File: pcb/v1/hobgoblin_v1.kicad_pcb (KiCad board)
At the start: 2 copper layers, 160 x 115 mm, 60 parts, among them J1 5V, J2 RC2014EXT1, J3 RC2014EXT2, J4 USB_B_Mini, J5 UART, SW1 RESET, SW2 ROMBNK, U1 74LS32, U10 FT232RL, U2 Z80CPU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

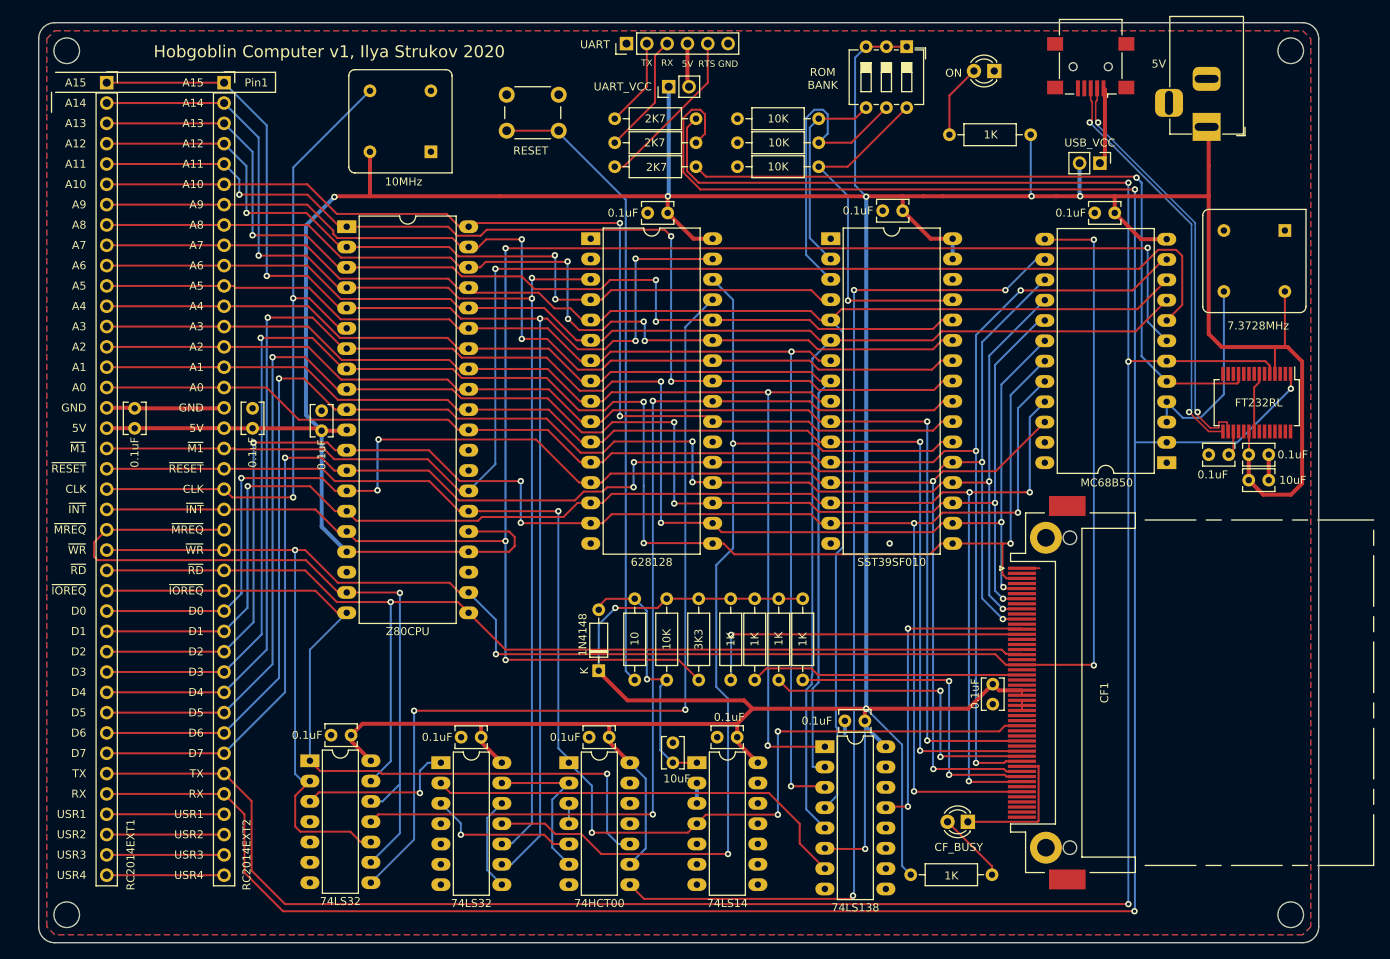
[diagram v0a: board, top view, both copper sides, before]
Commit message: Fix the CF card slot footprint (v1.1.)
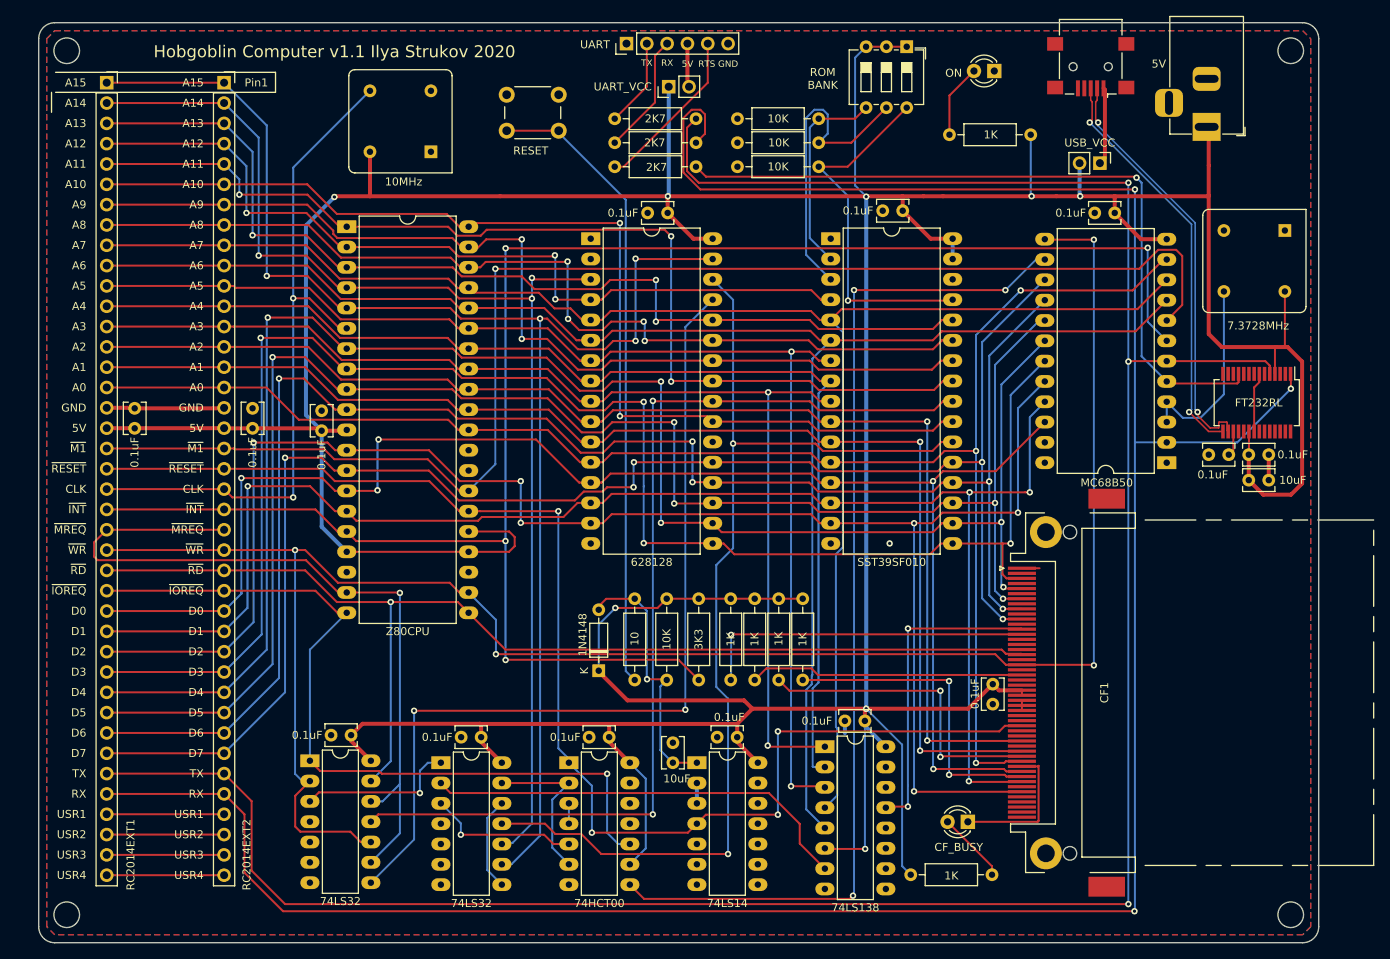
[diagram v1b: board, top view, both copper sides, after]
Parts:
- CF1: footprint Connector_Card:CF-Card_3M_N7E50-7516PK-20-WF -> hobgoblin:CF-Card_3M_N7E50-7516PK-20-WF
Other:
- rule pad_to_mask_clearance: 0.05 -> 0
- board text added: "Hobgoblin Computer v1.1 Ilya Strukov 2020"
- board text removed: "Hobgoblin Computer v1, Ilya Strukov 2020"

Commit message: Fix CF footprint pin numbering
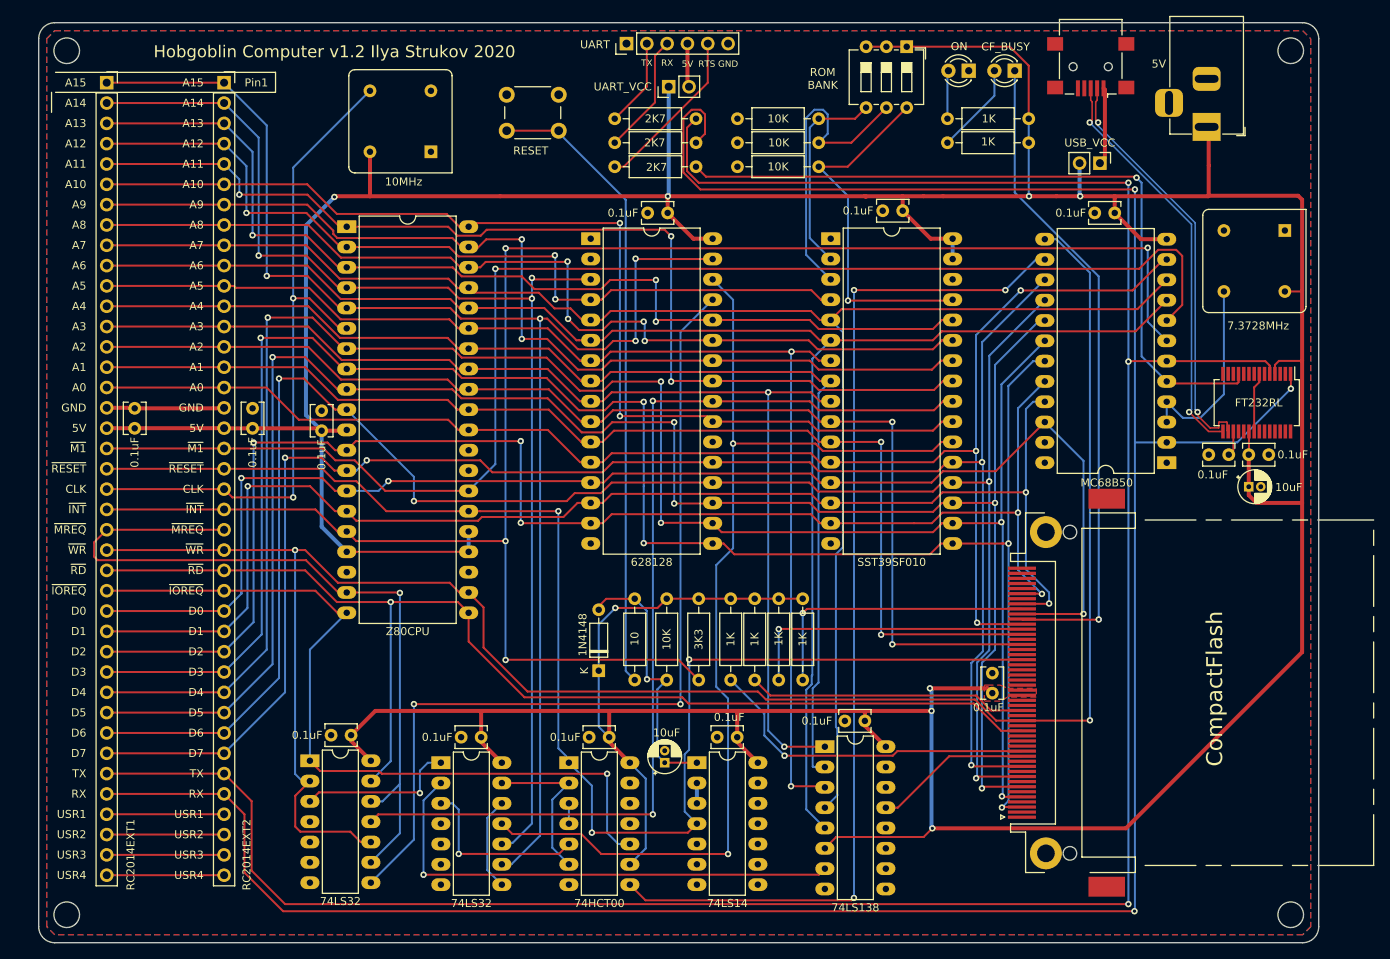
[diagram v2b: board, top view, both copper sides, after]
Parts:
- C1, C13: footprint Capacitor_THT:C_Disc_D3.8mm_W2.6mm_P2.50mm -> Capacitor_THT:CP_Radial_D4.0mm_P1.50mm
- moved D2 94.1 mm to (142.0, 26.0)
- moved R15 92.7 mm to (143.8, 35.0), turned to 180 degrees
- moved D5 3.20 mm to (136.2, 26.0)
- moved R11 2.02 mm to (143.8, 32.0)
- moved C16 1.12 mm to (139.2, 103.8), turned to 90 degrees
- moved C1 1.02 mm to (98.2, 112.5)
- moved C13 0.82 mm to (171.3, 78.0)
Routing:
- net Net-(CF1-Pad45): track 17.9 -> 82.6 mm, vias 0 -> 1
- net /D3: track 206.2 -> 236.3 mm, vias 4 -> 5
- net /D2: track 211.5 -> 182.3 mm, vias 6 -> 5
- net /D5: track 208.0 -> 234.7 mm
- net /D4: track 213.9 -> 240.2 mm
- net /D6: track 205.7 -> 229.8 mm, vias 5 -> 4
- net /D1: track 190.9 -> 167.2 mm, vias 4 -> 3
- net /D0: track 193.8 -> 172.3 mm, vias 5 -> 3
- net /~PORT10: track 39.4 -> 19.7 mm, vias 2 -> 0
- net VCC: track 674.4 -> 654.9 mm
- net /D7: track 198.0 -> 216.1 mm, vias 5 -> 4
- net /A0: track 201.1 -> 183.5 mm
- net /A1: track 158.1 -> 143.6 mm
- net /A2: track 159.4 -> 147.3 mm
- net /~RESET: track 166.0 -> 177.2 mm, vias 4 -> 3
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- added copper zone on F.Cu, net VCC
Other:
- board text added: "CompactFlash"
- board text added: "Hobgoblin Computer v1.2 Ilya Strukov 2020"
- board text removed: "Hobgoblin Computer v1.1 Ilya Strukov 2020"

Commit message: Reroute USB diff pair
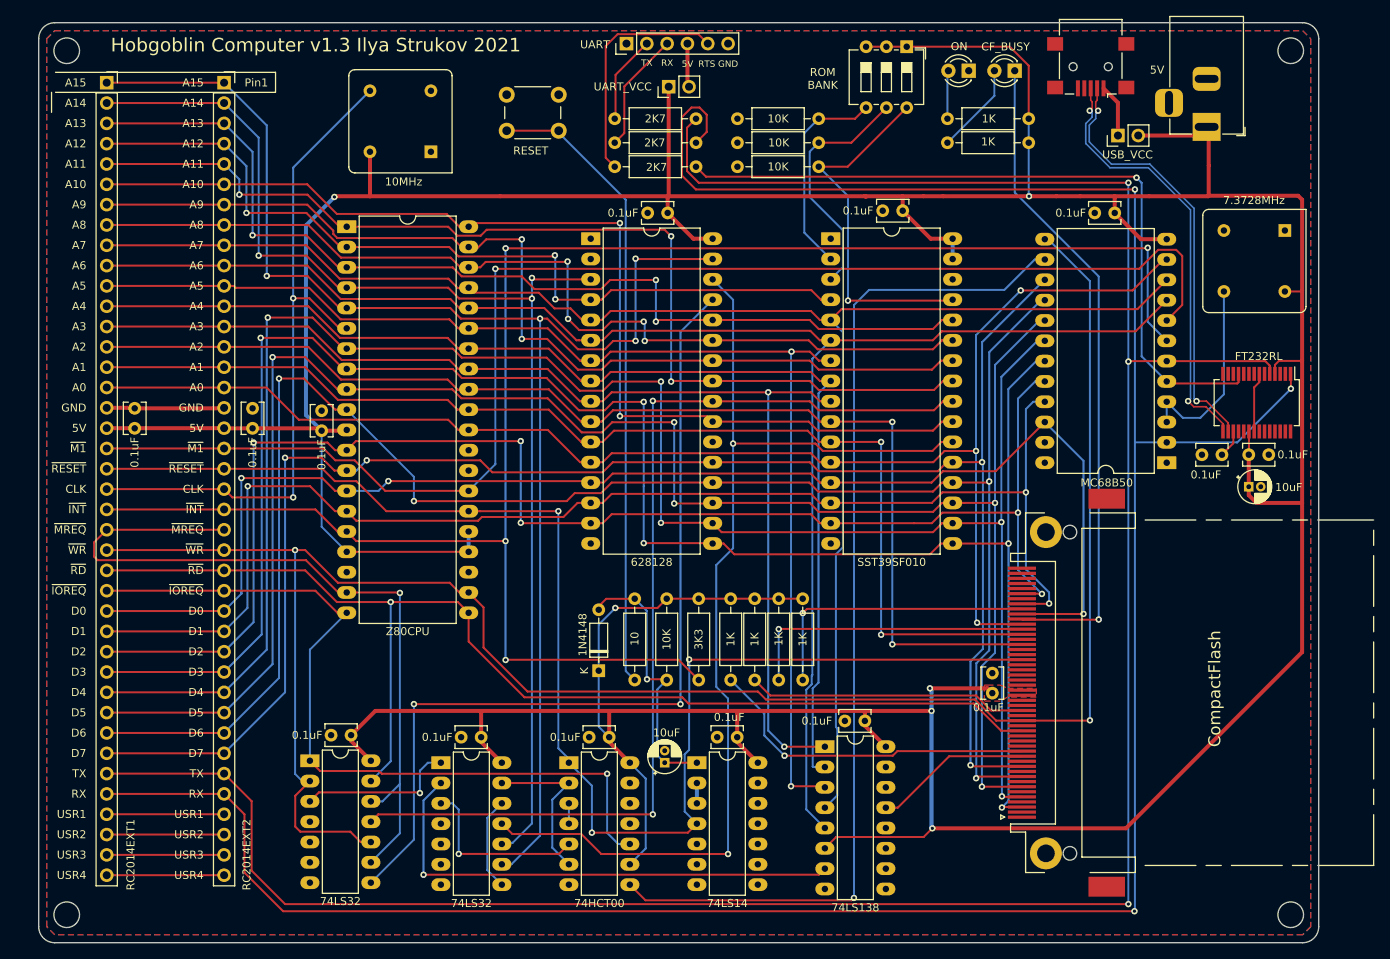
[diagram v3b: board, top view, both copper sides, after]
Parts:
- moved JP1 4.12 mm to (154.9, 34.1), turned to 90 degrees
- moved C15 0.85 mm to (165.4, 74.0)
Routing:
- net /ROMBNK1: track 39.1 -> 30.2 mm
- net Net-(J5-Pad5): track 20.9 -> 29.4 mm
- net VCC: track 654.9 -> 659.8 mm, vias 8 -> 6
- net /USB_UART/USBD+: track 51.3 -> 54.6 mm
- net Net-(J4-Pad1): track 9.69 -> 6.65 mm
- net /USB_UART/USBD-: track 52.5 -> 54.3 mm
- net /RXD: track 324.7 -> 325.9 mm
- net /IORQ: track 130.4 -> 129.3 mm, vias 3 -> 1
- net /D2: track 182.3 -> 183.0 mm
- net /~WR: track 244.9 -> 244.3 mm
- net /ROMBNK2: track 25.6 -> 26.1 mm
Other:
- board text added: "Hobgoblin Computer v1.3 Ilya Strukov 2021"
- board text removed: "Hobgoblin Computer v1.2 Ilya Strukov 2020"

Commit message: Fix IOWR/IORD pins on CF socket
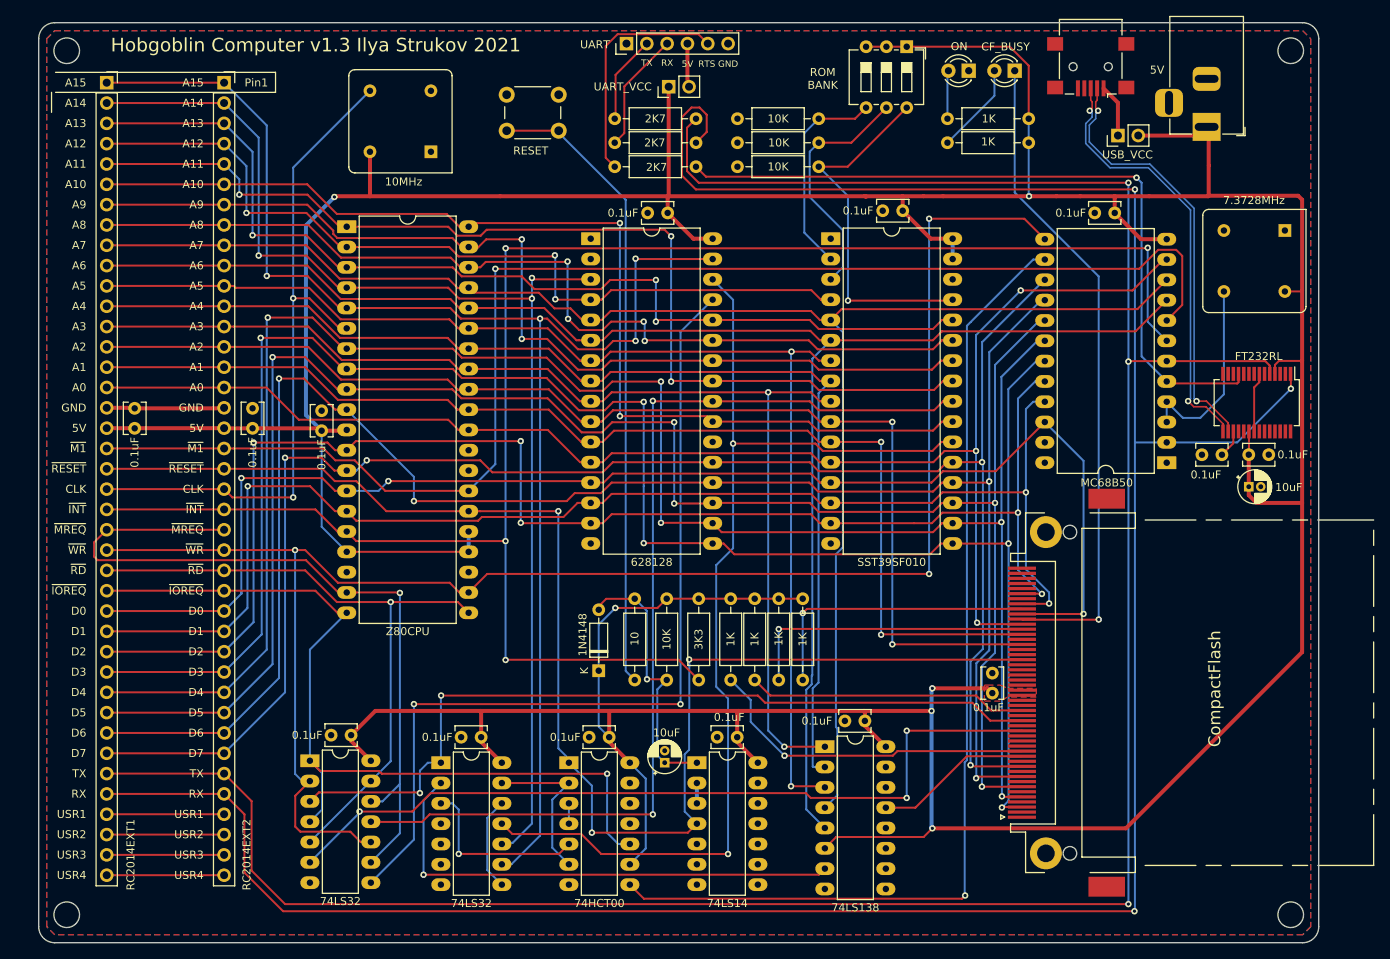
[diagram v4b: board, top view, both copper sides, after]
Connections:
- CF1 pad 34: /~RD -> /~IORD
- CF1 pad 35: /~WR -> /~IOWR
- U1 pad 4: (no net) -> /~IORQ
- U1 pad 5: (no net) -> /~RD
- U1 pad 6: (no net) -> /~IORD
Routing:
- net /~IORD: track 0.00 -> 101.3 mm, vias 0 -> 3
- net /~IOWR: track 20.1 -> 102.4 mm, vias 1 -> 2
- net /~RD: track 148.2 -> 81.6 mm
- net /~WR: track 244.3 -> 212.8 mm, vias 2 -> 3
- net /~IORQ: track 100.6 -> 109.5 mm
- net /IORQ: track 129.3 -> 127.3 mm

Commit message: Clean up routing
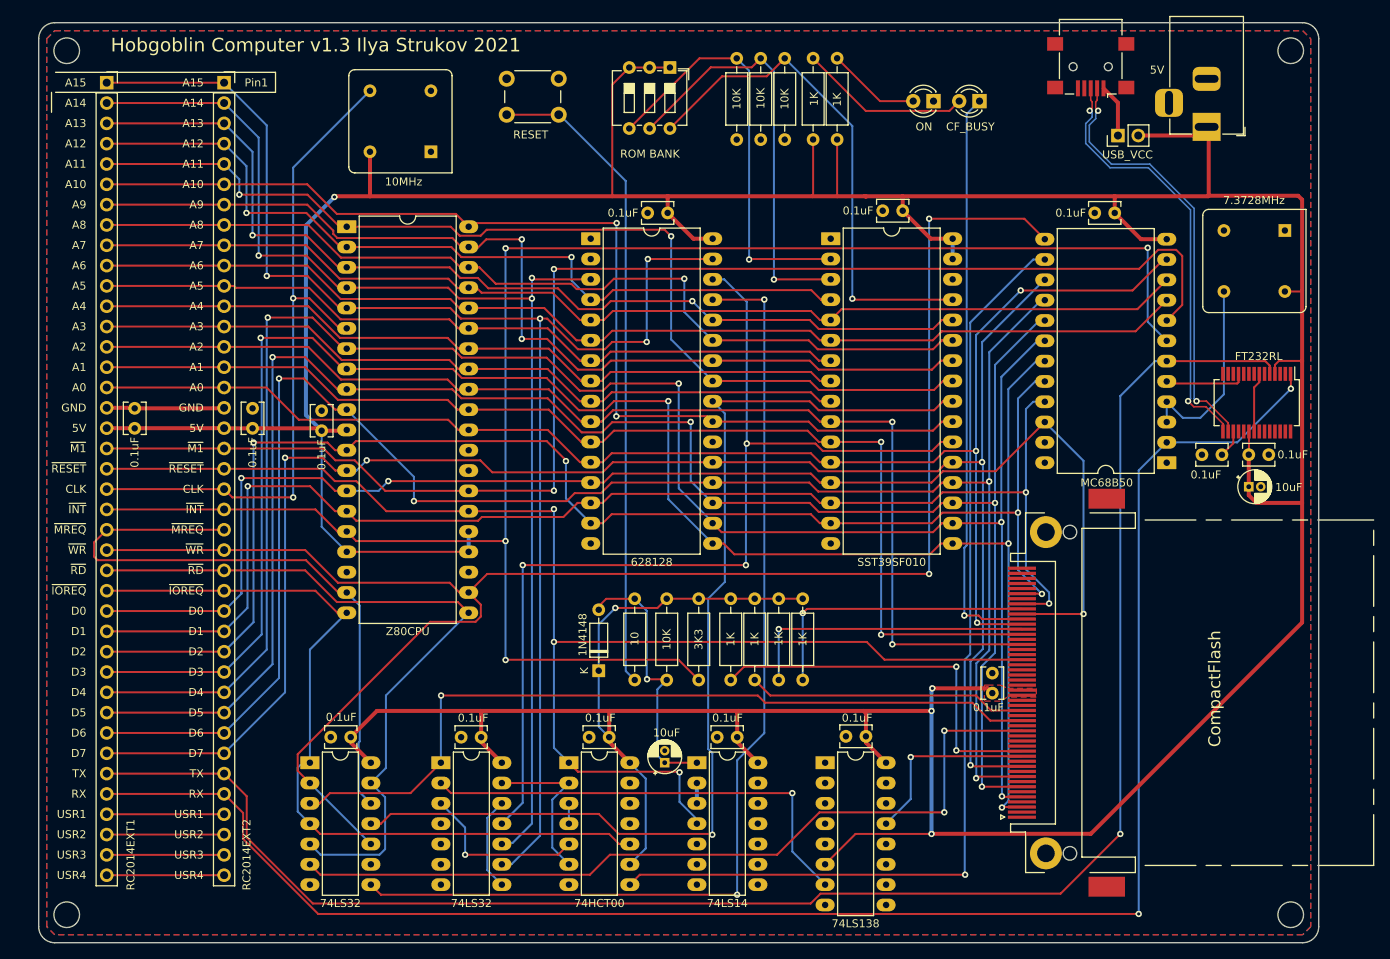
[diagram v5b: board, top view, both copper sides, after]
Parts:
- removed J5: UART, Connector_PinHeader_2.54mm:PinHeader_1x06_P2.54mm_Vertical
- removed JP2: UART_VCC, Connector_PinHeader_2.54mm:PinHeader_1x02_P2.54mm_Vertical
- removed R12, R13, R14: 2K7, Resistor_THT:R_Axial_DIN0207_L6.3mm_D2.5mm_P10.16mm_Horizontal
- moved SW2 29.7 mm to (98.9, 25.6)
- moved R15 27.0 mm to (116.8, 34.6), turned to 90 degrees
- moved R11 24.1 mm to (119.8, 34.6), turned to 90 degrees
- moved R6 14.2 mm to (113.2, 24.4), turned to 270 degrees
- moved R5 12.8 mm to (110.2, 24.4), turned to 270 degrees
- moved R4 12.7 mm to (107.2, 24.4), turned to 270 degrees
- moved D2 5.81 mm to (137.6, 29.8)
- moved D5 5.81 mm to (131.8, 29.8)
- moved U4 2.00 mm to (118.3, 112.5)
- moved SW1 2.00 mm to (78.5, 27.0)
- moved C10 1.93 mm to (123.4, 109.2)
- moved C12 0.25 mm to (59.0, 109.3)
- moved U1 0.25 mm to (53.9, 112.5)
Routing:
- net /RXD: track 325.9 -> 217.7 mm, vias 3 -> 2
- net /TXD: track 311.6 -> 216.5 mm, vias 3 -> 1
- net /~RTS: track 92.9 -> 10.2 mm, vias 1 -> 0
- net /A6: track 202.6 -> 139.4 mm
- net /A7: track 202.1 -> 139.4 mm
- net /A5: track 153.9 -> 95.3 mm, vias 2 -> 0
- net /A4: track 146.0 -> 95.3 mm
- net /A3: track 145.5 -> 95.3 mm, vias 2 -> 0
- net Net-(J5-Pad5): track 29.4 -> 0.00 mm
- net /ROMBNK2: track 26.1 -> 53.1 mm, vias 0 -> 1
- net /ROMBNK1: track 30.2 -> 53.0 mm, vias 0 -> 1
- net /ROMBNK0: track 45.4 -> 64.1 mm
- net /~MREQ: track 98.5 -> 79.8 mm, vias 1 -> 0
- net /~MEMWR: track 110.1 -> 128.6 mm
- net Net-(J5-Pad3): track 15.1 -> 0.00 mm
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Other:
- board text removed: "5V"
- board text removed: "GND"
- board text removed: "RTS"
- board text removed: "RX"
- board text removed: "TX"
